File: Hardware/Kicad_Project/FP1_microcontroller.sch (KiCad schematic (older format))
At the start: 38 parts

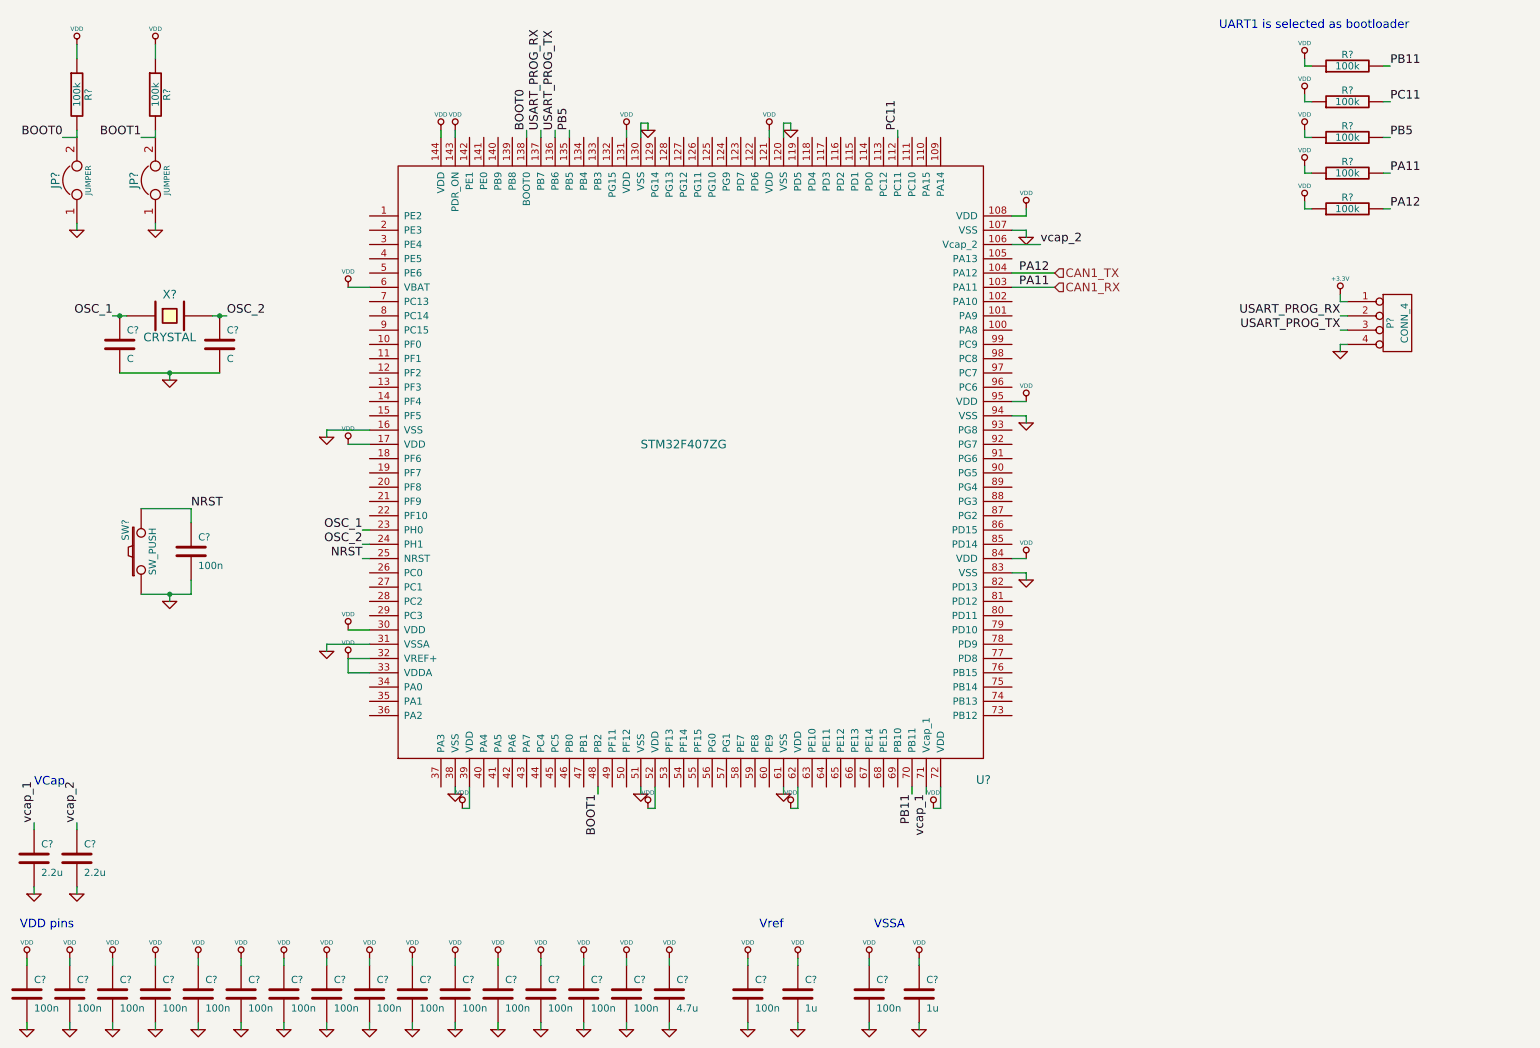
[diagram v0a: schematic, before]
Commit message: [Hardware] Add two USART interface and begin the SD card schematic
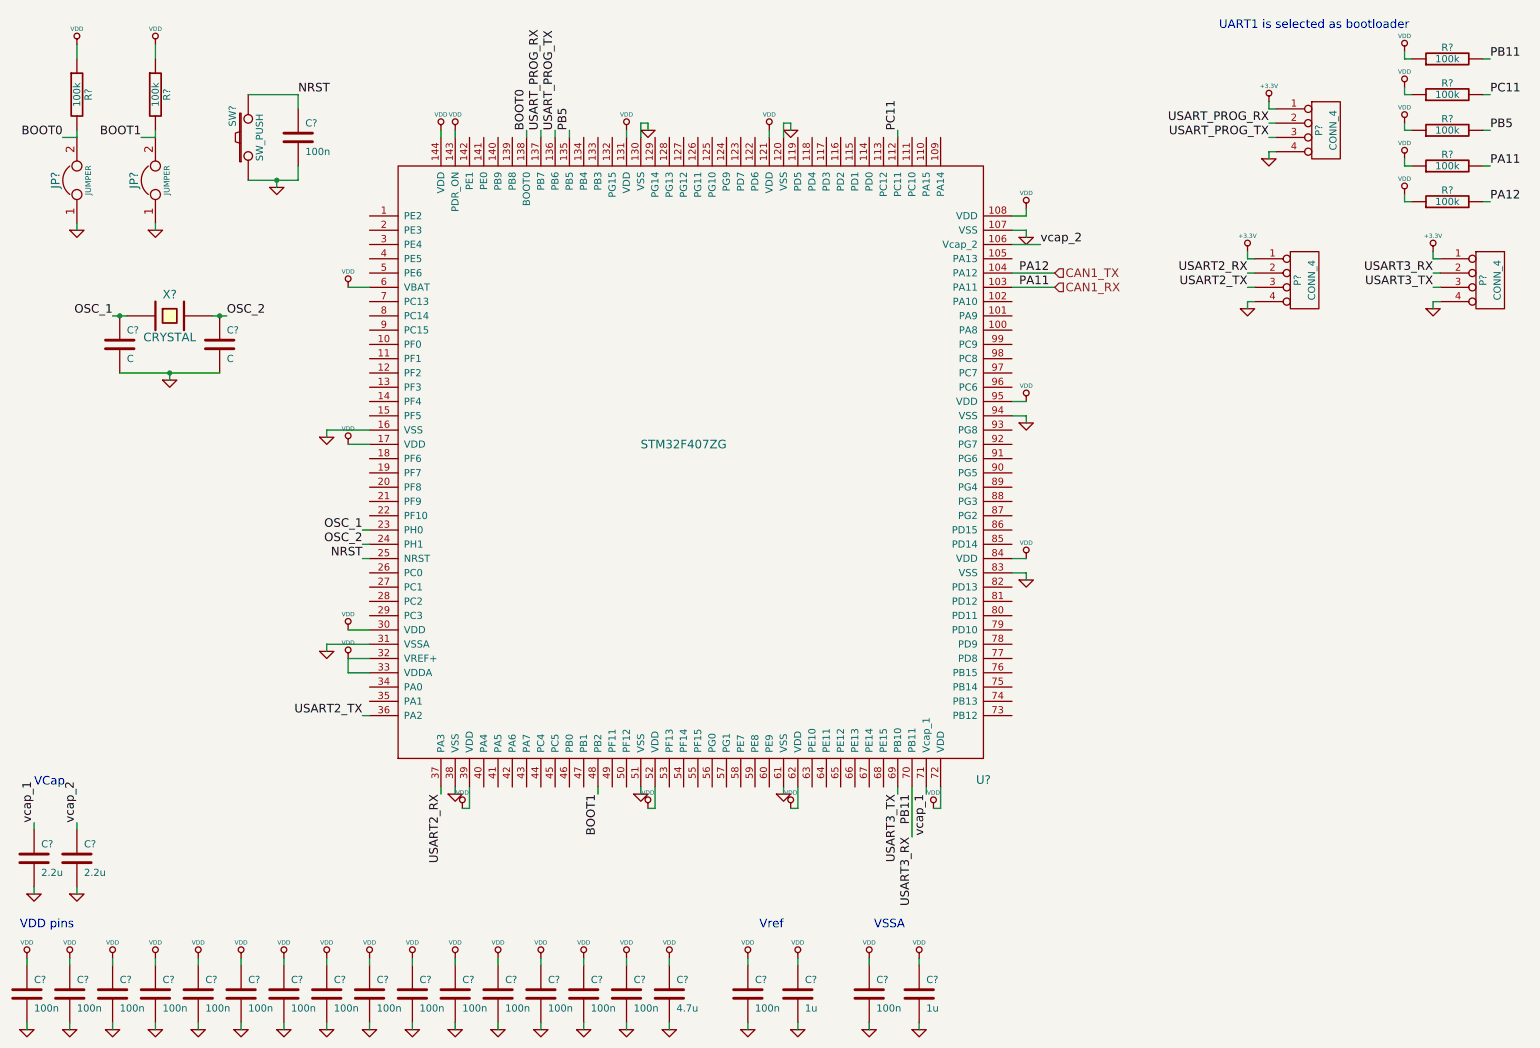
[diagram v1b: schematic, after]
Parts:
- added P? (x2): CONN_4, symbol CONN_4
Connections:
- net +3.3V: now also P?.1 (P1), P?.1 (P1)
- net GND: now also P?.4 (P4), P?.4 (P4)
- net PB11: now also P?.2 (P2)
- net USART2_TX: now reaches U?.36 (PA2)
- net USART2_TX: now also P?.3 (P3)
- net USART2_RX: now reaches U?.37 (PA3)
- net USART2_RX: now also P?.2 (P2)
- net USART3_TX: now reaches U?.69 (PB10)
- net USART3_TX: now also P?.3 (P3)
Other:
- moved on the sheet: C?, P?, R?, SW?
